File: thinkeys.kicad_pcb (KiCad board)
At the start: 2 copper layers, 363.7 x 279.2 mm, 379 parts, among them J1 Pointing stick, J2 Pointing stick, J3 PWRSWITCH, SW1 SW_Push, SW10 SW_Push, SW11 SW_Push, SW12 SW_Push, SW13 SW_Push, SW14 SW_Push, SW15 SW_Push, SW16 SW_Push, SW17 SW_Push, SW18 SW_Push, SW19 SW_Push, SW2 SW_Push, SW20 SW_Push, SW21 SW_Push, SW22 SW_Push, SW23 SW_Push, SW24 SW_Push, SW25 SW_Push, SW26 SW_Push, SW27 SW_Push, SW28 SW_Push, SW29 SW_Push, SW3 SW_Push, SW30 SW_Push, SW31 SW_Push, SW32 SW_Push, SW33 SW_Push, SW34 SW_Push, SW35 SW_Push, SW36 SW_Push, SW37 SW_Push, SW38 SW_Push, SW39 SW_Push, SW4 SW_Push, SW40 SW_Push, SW41 SW_Push, SW42 SW_Push, SW43 SW_Push, SW44 SW_Push, SW45 SW_Push, SW46 SW_Push, SW47 SW_Push, SW48 SW_Push, SW49 SW_Push, SW5 SW_Push, SW50 SW_Push, SW51 SW_Push, SW54 SW_Push, SW55 SW_Push, SW56 SW_Push, SW57 SW_Push, SW58 SW_Push, SW59 SW_Push, SW6 SW_Push, SW60 SW_Push, SW61 SW_Push, SW62 SW_Push, SW63 SW_Push, SW64 SW_Push, SW65 SW_Push, SW66 SW_Push, SW69 SW_Push, SW7 SW_Push, SW70 SW_Push, SW71 SW_Push, SW72 SW_Push, SW73 SW_Push, SW74 SW_Push, SW75 SW_Push, SW76 SW_Push, SW77 SW_Push, SW78 SW_Push, SW79 SW_Push, SW8 SW_Push, SW80 SW_Push, SW81 SW_Push, SW82 SW_Push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

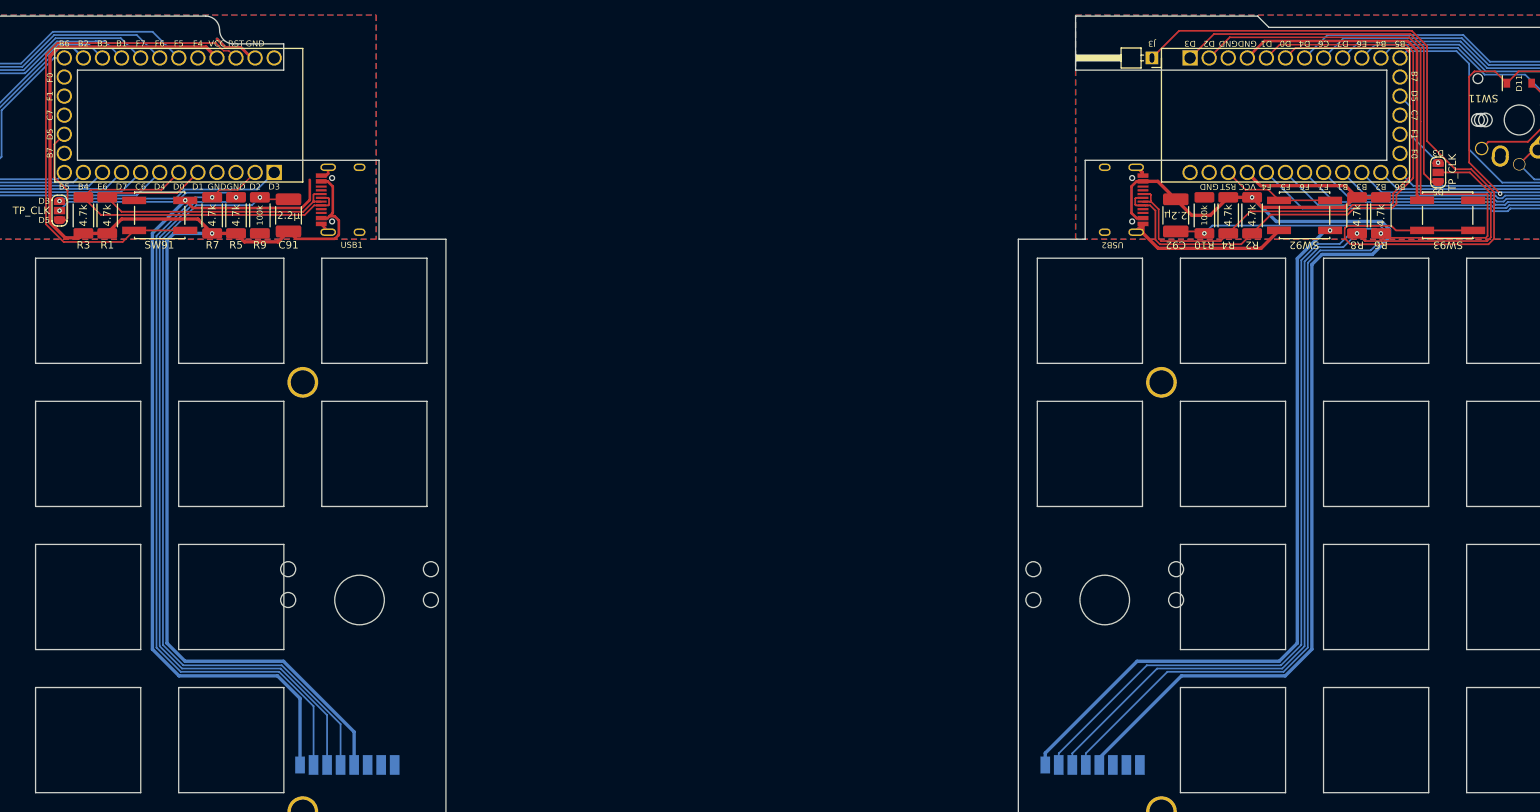
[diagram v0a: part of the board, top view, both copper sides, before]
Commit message: switch to 1206 compoments and add lcsc part number
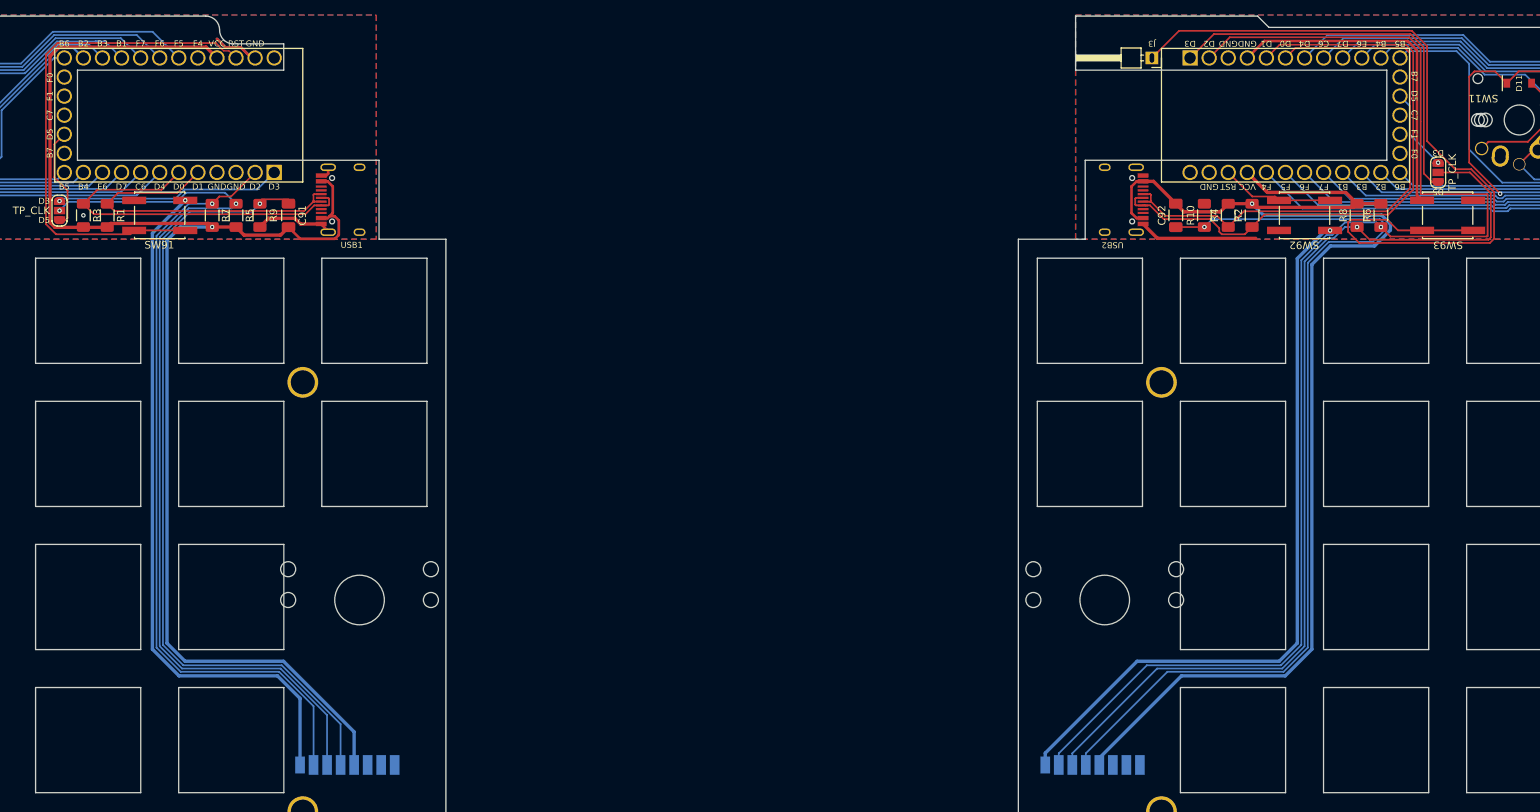
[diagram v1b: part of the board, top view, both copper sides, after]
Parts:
- C91, C92: footprint Capacitor_SMD:C_1812_4532Metric_Pad1.57x3.40mm_HandSolder -> Capacitor_SMD:C_1206_3216Metric_Pad1.33x1.80mm_HandSolder
- R1, R10, R2, R3, R4, R5, R6, R7, R8, R9: footprint Resistor_SMD:R_2010_5025Metric_Pad1.40x2.65mm_HandSolder -> Resistor_SMD:R_1206_3216Metric_Pad1.30x1.75mm_HandSolder
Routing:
- net GND1: track 126.9 -> 115.7 mm, vias 1 -> 2
- net GND2: track 166.6 -> 158.7 mm
- net /right/SCL: track 80.1 -> 76.5 mm
- net /right/SDA: track 85.3 -> 82.4 mm
- net VCC: track 193.8 -> 191.5 mm
- net /right/DATA: track 181.0 -> 182.4 mm
- net VDD: track 178.2 -> 176.8 mm
- net /left/RST: track 70.1 -> 69.3 mm
- net Net-(C91-Pad1): track 106.6 -> 105.9 mm
- net Net-(C92-Pad1): track 129.0 -> 129.6 mm
- net /right/CLK: track 130.6 -> 131.1 mm

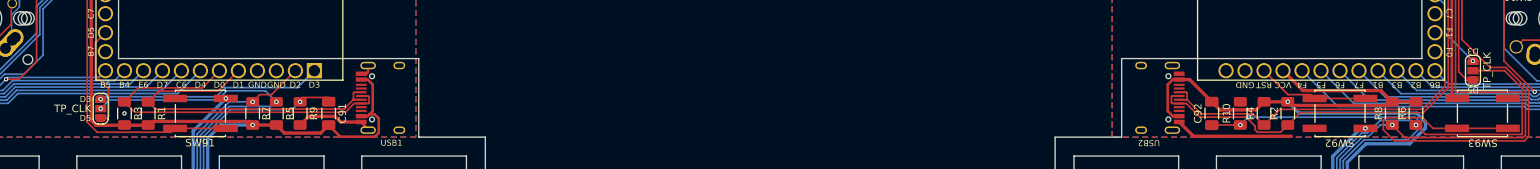
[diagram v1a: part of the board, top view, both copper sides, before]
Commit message: pcb: label jumpers as JP**
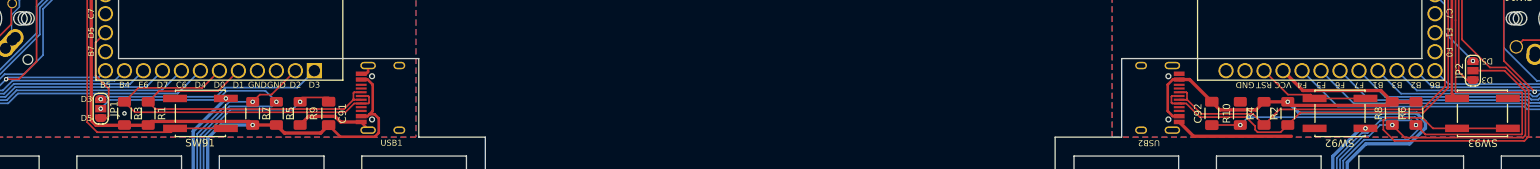
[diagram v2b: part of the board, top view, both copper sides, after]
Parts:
- JP1, JP2: footprint libmodulo:SolderJumper-3_P1.3mm_Open_RoundedPad1.0x1.5mm_NumberLabels -> Jumper:SolderJumper-3_P1.3mm_Open_RoundedPad1.0x1.5mm_NumberLabels

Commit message: add led
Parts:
- added J4: Conn_01x03_Male, Connector_PinHeader_2.00mm:PinHeader_1x03_P2.00mm_Vertical_SMD_Pin1Left, F.Cu at (70.5, -12.7)
- added L1: LED_Small, LED_SMD:LED_0805_2012Metric_Pad1.15x1.40mm_HandSolder, F.Cu at (69.8, -11.7)
- moved JP1 6.35 mm to (68.6, -18.4)
- moved JP2 0.63 mm to (255.3, -18.4)
- moved R6 0.63 mm to (248.9, -12.7)
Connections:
- U1 pad 20: (no net) -> Net-(J4-Pad2)
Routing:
- net Net-(J4-Pad2): track 0.00 -> 48.0 mm
- net VCC: track 191.5 -> 216.8 mm
- net GND2: track 158.7 -> 142.9 mm
- net Net-(JP1-Pad1): track 30.2 -> 40.8 mm
- net /left/RST: track 69.3 -> 79.2 mm
- net GND1: track 115.7 -> 107.7 mm
- net /left/CLK: track 124.2 -> 132.1 mm
- net Net-(JP1-Pad3): track 13.6 -> 9.41 mm
- net /right/c3: track 104.4 -> 103.2 mm
- net /left/r1: track 37.8 -> 36.5 mm
- net /right/c0: track 72.1 -> 70.8 mm
- net /left/c5: track 74.6 -> 73.3 mm
- net /left/c2: track 98.4 -> 97.2 mm
- net /right/r4: track 64.8 -> 63.5 mm
- net /right/c6: track 128.4 -> 127.1 mm
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
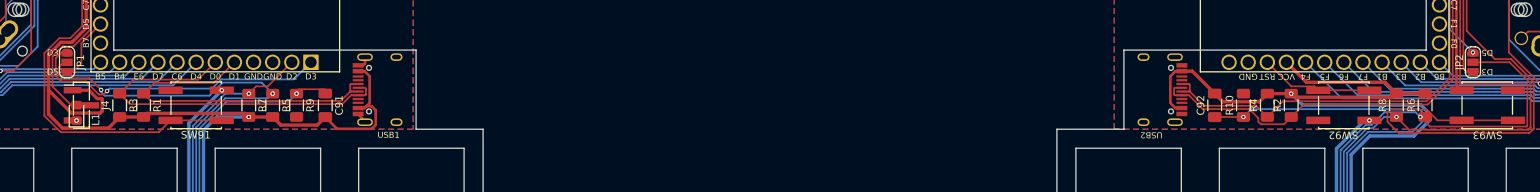
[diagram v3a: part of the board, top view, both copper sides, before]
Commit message: pcb: fix text and footprint location
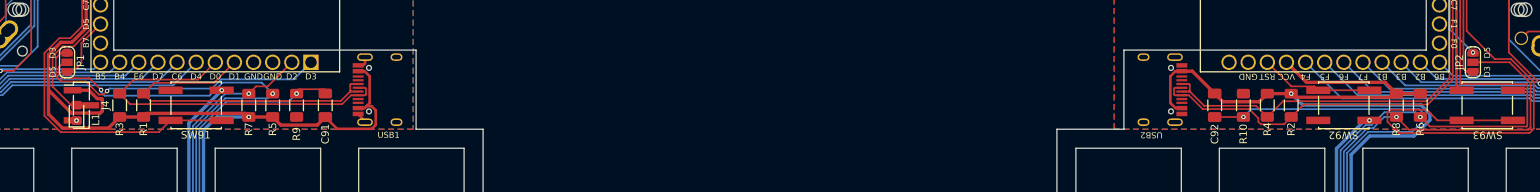
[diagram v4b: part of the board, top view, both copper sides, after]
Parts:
- moved R6 0.63 mm to (248.3, -12.7)

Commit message: prevent text issues, new footprints/3dmodels
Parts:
- removed the Ref** at (200.5, 235.2)
- removed the Ref** at (232.6, 172.1)
- removed the Ref** at (124.3, 235.2)
- added ?: , , F.Cu at (124.3, 235.2)
- added ?: , , F.Cu at (200.5, 235.2)
- added ?: , , F.Cu at (232.6, 172.1)
- USB1, USB2: footprint libmodulo:HRO-TYPE-C-31-M-12 -> libmodulo:USB_C_Receptacle_HRO_TYPE-C-31-M-12
- moved USB1 3.65 mm to (111.3, -14.8)
- moved USB2 3.65 mm to (212.6, -14.8)
- moved L1 0.24 mm to (70.0, -11.8)
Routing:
- net VCC: track 216.8 -> 216.1 mm
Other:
- board text added: "Caps Lock"

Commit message: pcb: extend usb port, adjust copper to match
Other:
- outline, holes or cut-outs redrawn

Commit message: move push button references to S**, text to side
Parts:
- gave numbers to parts that had none: 54
- renumbered SW91 to S1, SW92 to S2, SW93 to S3
